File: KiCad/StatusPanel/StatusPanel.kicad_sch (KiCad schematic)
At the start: 37 parts, among them J1 CONN, J10 CONN_12V_CTL, J11 CONN_12V_GND, J12 CONN_TASK_CTL, J13 CONN_TASK_GND, J14 CONN_5V_CTL, J15 CONN_5V_GND, J16 CONN_COM_CTL, J17 CONN_COM_GND, J18 CONN_LOW_CTL, J19 CONN_LOW_GND, J2 CONN_RESET_CTL, J20 CONN_ERROR_CTL, J21 CONN_ERROR_GND, J22 CONN_7SEG, J3 CONN_RESET_GND, J4 CONN_USB_5V, J5 CONN_USB_CTL, J6 CONN_INPUT_CTL, J7 CONN_INPUT_GND, J8 CONN_RS485_CTL, J9 CONN_RS485_GND, U1 2281SB, U2 TM1637

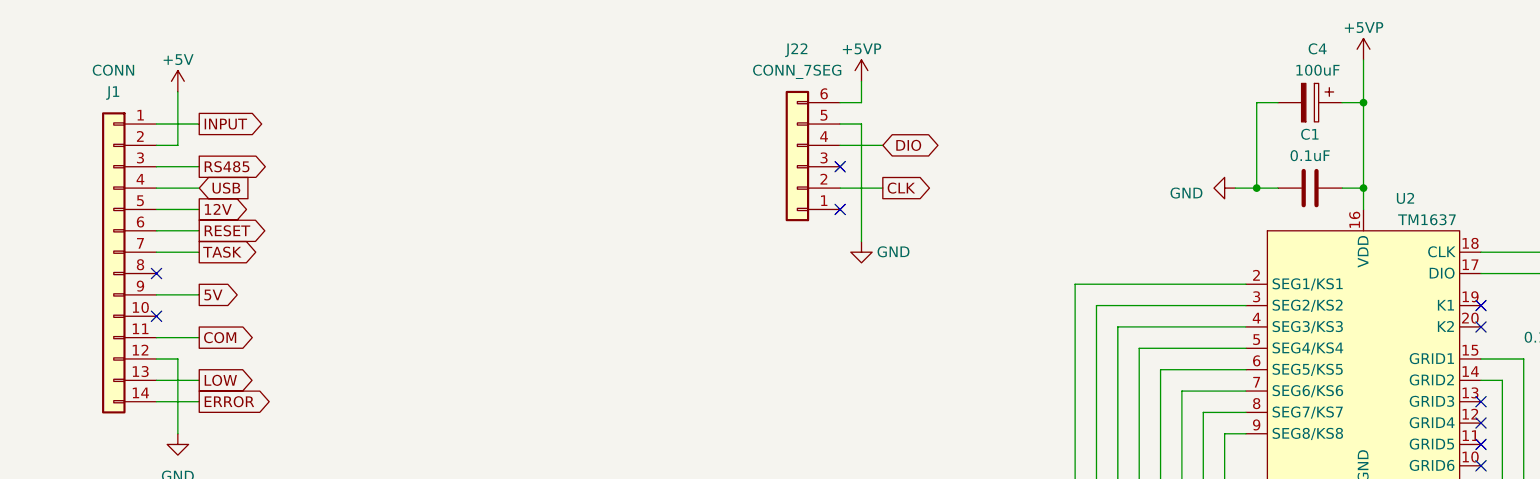
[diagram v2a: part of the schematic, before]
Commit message: 7セグ用コネクタを6Pから14Pの空いているピンに押し込んだ
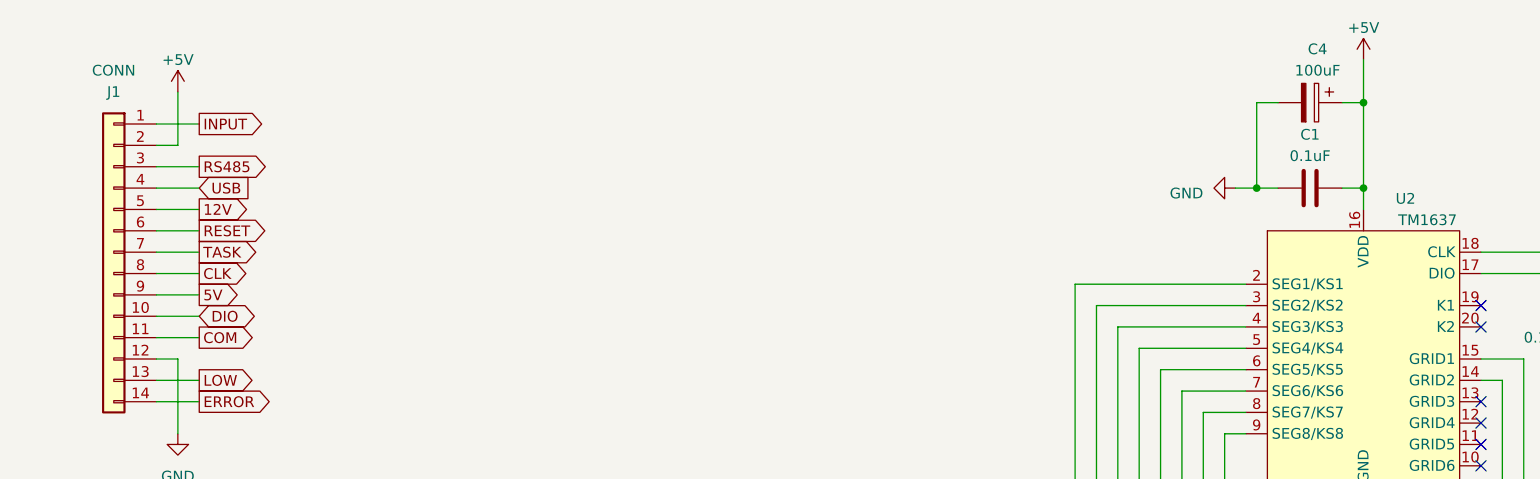
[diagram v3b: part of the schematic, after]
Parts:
- removed J22: CONN_7SEG, TSRP_Connector_Hirose:DF51A-6DP-2DSA, symbol Connector_Generic:Conn_01x06
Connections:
- net +5VP is gone; now on net +5V: C1.2, C4.1, U2.16 (VDD)
- net CLK: now also J1.8 (Pin_8)
- net DIO: now also J1.10 (Pin_10)
- no-connect marks 10 -> 6
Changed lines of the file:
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@@
   (junction (at 212.09 34.29) (diameter 0) (color 0 0 0 0)
   )
-  (no_connect (at 149.86 46.99))
   (no_connect (at 226.06 69.85))
-  (no_connect (at 68.58 59.69))
   (no_connect (at 226.06 58.42))
   (no_connect (at 226.06 74.93))
-  (no_connect (at 149.86 41.91))
   (no_connect (at 226.06 72.39))
   (no_connect (at 226.06 77.47))
-  (no_connect (at 68.58 54.61))
   (no_connect (at 226.06 60.96))
   (wire (pts (xy 53.34 149.86) (xy 55.88 149.86))
@@
     (stroke (width 0) (type default))
   )
+  (wire (pts (xy 68.58 54.61) (xy 73.66 54.61))
+    (stroke (width 0) (type default))
+  )
   (wire (pts (xy 209.55 44.45) (xy 212.09 44.45))
     (stroke (width 0) (type default))
   )
-  (wire (pts (xy 152.4 50.8) (xy 152.4 36.83))
-    (stroke (width 0) (type default))
-  )
   (wire (pts (xy 240.03 64.77) (xy 240.03 67.31))
     (stroke (width 0) (type default))
@@
     (stroke (width 0) (type default))
   )
-  (wire (pts (xy 149.86 36.83) (xy 152.4 36.83))
-    (stroke (width 0) (type default))
-  )
   (wire (pts (xy 53.34 109.22) (xy 55.88 109.22))
     (stroke (width 0) (type default))
@@
     (stroke (width 0) (type default))
   )
-  (wire (pts (xy 149.86 34.29) (xy 152.4 34.29))
-    (stroke (width 0) (type default))
-  )
   (wire (pts (xy 177.8 106.68) (xy 204.47 106.68))
     (stroke (width 0) (type default))
@@
     (stroke (width 0) (type default))
   )
-  (wire (pts (xy 149.86 39.37) (xy 154.94 39.37))
-    (stroke (width 0) (type default))
-  )
   (wire (pts (xy 198.12 73.66) (xy 195.58 73.66))
     (stroke (width 0) (type default))
@@
     (stroke (width 0) (type default))
   )
-  (wire (pts (xy 149.86 44.45) (xy 154.94 44.45))
-    (stroke (width 0) (type default))
-  )
   (wire (pts (xy 68.58 62.23) (xy 73.66 62.23))
     (stroke (width 0) (type default))
@@
     (stroke (width 0) (type default))
   )
-  (wire (pts (xy 152.4 31.75) (xy 152.4 34.29))
-    (stroke (width 0) (type default))
-  )
   (wire (pts (xy 226.06 67.31) (xy 228.6 67.31))
     (stroke (width 0) (type default))
@@
   )
   (wire (pts (xy 95.25 109.22) (xy 97.79 109.22))
+    (stroke (width 0) (type default))
+  )
+  (wire (pts (xy 68.58 59.69) (xy 73.66 59.69))
     (stroke (width 0) (type default))
   )
@@
     )
   )
+  (global_label "DIO" (shape bidirectional) (at 73.66 59.69 0) (fields_autoplaced)
+    (effects (font (size 1.27 1.27)) (justify left))
+    (property "Intersheetrefs" "${INTERSHEET_REFS}" (at 80.8824 59.69 0)
+      (effects (font (size 1.27 1.27)) (justify left) hide)
+    )
+  )
   (global_label "USB" (shape output) (at 97.79 109.22 0) (fields_autoplaced)
     (effects (font (size 1.27 1.27)) (justify left))
@@
     )
   )
+  (global_label "CLK" (shape output) (at 73.66 54.61 0) (fields_autoplaced)
+    (effects (font (size 1.27 1.27)) (justify left))
+    (property "Intersheetrefs" "${INTERSHEET_REFS}" (at 80.1339 54.61 0)
+      (effects (font (size 1.27 1.27)) (justify left) hide)
+    )
+  )
   (global_label "INPUT" (shape input) (at 43.18 123.19 180) (fields_autoplaced)
     (effects (font (size 1.27 1.27)) (justify right))
@@
     )
   )
-  (global_label "CLK" (shape output) (at 154.94 44.45 0) (fields_autoplaced)
-    (effects (font (size 1.27 1.27)) (justify left))
-    (property "Intersheetrefs" "${INTERSHEET_REFS}" (at 161.4139 44.45 0)
-      (effects (font (size 1.27 1.27)) (justify left) hide)
-    )
-  )
-  (global_label "DIO" (shape bidirectional) (at 154.94 39.37 0) (fields_autoplaced)
-    (effects (font (size 1.27 1.27)) (justify left))
-    (property "Intersheetrefs" "${INTERSHEET_REFS}" (at 162.1624 39.37 0)
-      (effects (font (size 1.27 1.27)) (justify left) hide)
-    )
-  )
   (global_label "TASK" (shape input) (at 43.18 149.86 180) (fields_autoplaced)
     (effects (font (size 1.27 1.27)) (justify right))
@@
         (path "/4e417ca2-390b-4eb8-b376-7083d40608de"
           (reference "C2") (unit 1)
-        )
-      )
-    )
-  )
-  (symbol (lib_id "power:+5VP") (at 212.09 29.21 0) (unit 1)
-    (in_bom yes) (on_board yes) (dnp no) (fields_autoplaced)
-    (property "Reference" "#PWR013" (at 212.09 33.02 0)
-      (effects (font (size 1.27 1.27)) hide)
-    )
-    (property "Value" "+5VP" (at 212.09 25.4 0)
-      (effects (font (size 1.27 1.27)))
-    )
-    (property "Footprint" "" (at 212.09 29.21 0)
-      (effects (font (size 1.27 1.27)) hide)
-    )
-    (property "Datasheet" "" (at 212.09 29.21 0)
-      (effects (font (size 1.27 1.27)) hide)
-    )
-    (pin "1")
-    (instances
-      (project "StatusPanel"
-        (path "/4e417ca2-390b-4eb8-b376-7083d40608de"
-          (reference "#PWR013") (unit 1)
         )
       )
@@
     )
   )
-  (symbol (lib_id "power:GND") (at 152.4 50.8 0) (mirror y) (unit 1)
-    (in_bom yes) (on_board yes) (dnp no)
-    (property "Reference" "#PWR014" (at 152.4 57.15 0)
-      (effects (font (size 1.27 1.27)) hide)
-    )
-    (property "Value" "GND" (at 156.21 52.07 0)
-      (effects (font (size 1.27 1.27)))
-    )
-    (property "Footprint" "" (at 152.4 50.8 0)
-      (effects (font (size 1.27 1.27)) hide)
-    )
-    (property "Datasheet" "" (at 152.4 50.8 0)
-      (effects (font (size 1.27 1.27)) hide)
-    )
-    (pin "1")
-    (instances
-      (project "StatusPanel"
-        (path "/4e417ca2-390b-4eb8-b376-7083d40608de"
-          (reference "#PWR014") (unit 1)
-        )
-      )
-      (project "LaunchController"
-        (path "/628d040b-43bf-4733-804f-091644a90124"
-          (reference "#PWR044") (unit 1)
-        )
-      )
-    )
-  )
   (symbol (lib_id "Connector_Generic:Conn_01x01") (at 60.96 158.75 0) (unit 1)
     (in_bom yes) (on_board yes) (dnp no)
@@
         (path "/4e417ca2-390b-4eb8-b376-7083d40608de"
           (reference "J10") (unit 1)
+        )
+      )
+    )
+  )
+  (symbol (lib_id "power:+5V") (at 212.09 29.21 0) (unit 1)
+    (in_bom yes) (on_board yes) (dnp no) (fields_autoplaced)
+    (property "Reference" "#PWR013" (at 212.09 33.02 0)
+      (effects (font (size 1.27 1.27)) hide)
+    )
+    (property "Value" "+5V" (at 212.09 25.4 0)
+      (effects (font (size 1.27 1.27)))
+    )
+    (property "Footprint" "" (at 212.09 29.21 0)
+      (effects (font (size 1.27 1.27)) hide)
+    )
+    (property "Datasheet" "" (at 212.09 29.21 0)
+      (effects (font (size 1.27 1.27)) hide)
+    )
+    (pin "1")
+    (instances
+      (project "StatusPanel"
+        (path "/4e417ca2-390b-4eb8-b376-7083d40608de"
+          (reference "#PWR013") (unit 1)
         )
       )
@@
     )
   )
-  (symbol (lib_id "Connector_Generic:Conn_01x06") (at 144.78 41.91 180) (unit 1)
-    (in_bom yes) (on_board yes) (dnp no)
-    (property "Reference" "J22" (at 144.78 27.94 0)
-      (effects (font (size 1.27 1.27)))
-    )
-    (property "Value" "CONN_7SEG" (at 144.78 30.48 0)
-      (effects (font (size 1.27 1.27)))
-    )
-    (property "Footprint" "TSRP_Connector_Hirose:DF51A-6DP-2DSA" (at 144.78 41.91 0)
-      (effects (font (size 1.27 1.27)) hide)
-    )
-    (property "Datasheet" "~" (at 144.78 41.91 0)
-      (effects (font (size 1.27 1.27)) hide)
-    )
-    (pin "1")
-    (pin "2")
-    (pin "3")
-    (pin "4")
-    (pin "5")
-    (pin "6")
-    (instances
-      (project "StatusPanel"
-        (path "/4e417ca2-390b-4eb8-b376-7083d40608de"
-          (reference "J22") (unit 1)
-        )
-      )
-      (project "LaunchController"
-        (path "/628d040b-43bf-4733-804f-091644a90124"
-          (reference "J13") (unit 1)
-        )
-      )
-    )
-  )
   (symbol (lib_id "Connector_Generic:Conn_01x01") (at 80.01 140.97 180) (unit 1)
     (in_bom yes) (on_board yes) (dnp no) (fields_autoplaced)
@@
         )
       )
-    )
-  )
-  (symbol (lib_id "power:+5VP") (at 152.4 31.75 0) (unit 1)
-    (in_bom yes) (on_board yes) (dnp no) (fields_autoplaced)
-    (property "Reference" "#PWR020" (at 152.4 35.56 0)
-      (effects (font (size 1.27 1.27)) hide)
-    )
-    (property "Value" "+5VP" (at 152.4 27.94 0)
-      (effects (font (size 1.27 1.27)))
-    )
-    (property "Footprint" "" (at 152.4 31.75 0)
-      (effects (font (size 1.27 1.27)) hide)
-    )
-    (property "Datasheet" "" (at 152.4 31.75 0)
-      (effects (font (size 1.27 1.27)) hide)
-    )
-    (pin "1")
-    (instances
-      (project "StatusPanel"
-        (path "/4e417ca2-390b-4eb8-b376-7083d40608de"
-          (reference "#PWR020") (unit 1)
-        )
-      )

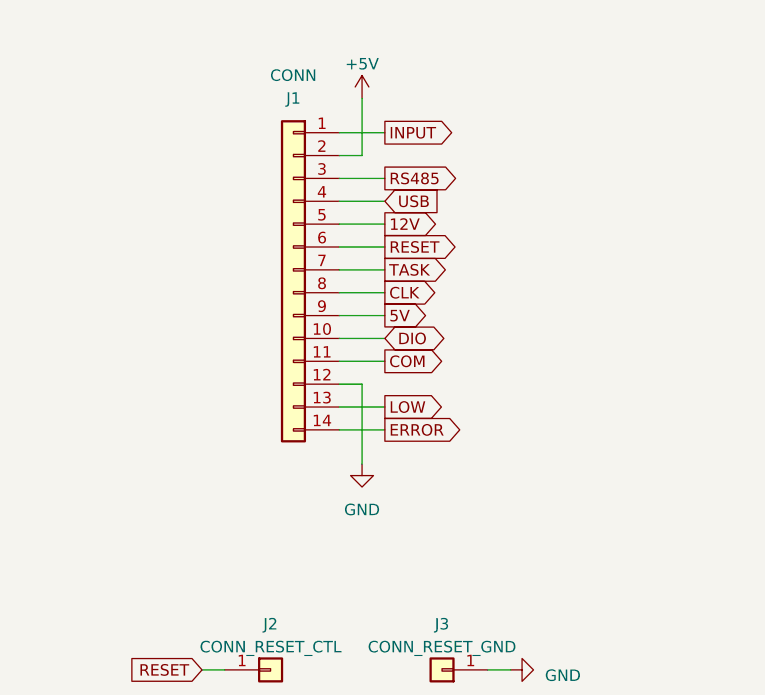
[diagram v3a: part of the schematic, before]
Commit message: ステータスパネルのコネクタをDF11に変更
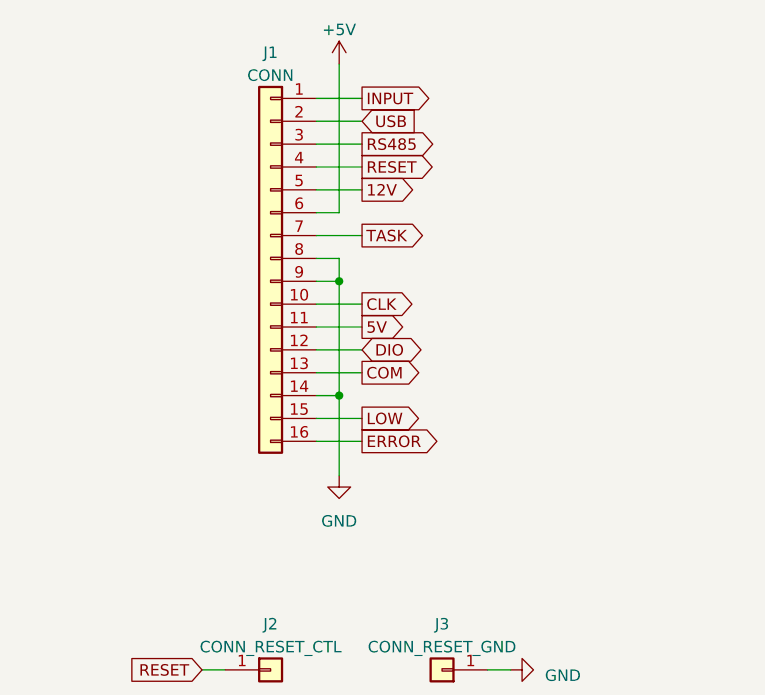
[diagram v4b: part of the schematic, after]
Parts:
- removed J1: CONN, TSRP_Connector_Hirose:DF51A-14DP-2DS, symbol Connector_Generic:Conn_01x14
- added J1: CONN, TSRP_Connector_Hirose:DF11CZ-16DP-2V, symbol Connector_Generic:Conn_01x16
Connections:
- net +5V: now also J1.6 (Pin_6)
- net 12V: now also J1.5 (Pin_5)
- net 5V: now also J1.11 (Pin_11)
- net CLK: now also J1.10 (Pin_10)
- net COM: now also J1.13 (Pin_13)
- net DIO: now also J1.12 (Pin_12)
- net ERROR: now also J1.16 (Pin_16)
- net GND: now also J1.14 (Pin_14), J1.8 (Pin_8), J1.9 (Pin_9)
- net INPUT: now also J1.1 (Pin_1)
- net LOW: now also J1.15 (Pin_15)
- net RESET: now also J1.4 (Pin_4)
- net RS485: now also J1.3 (Pin_3)
- net TASK: now also J1.7 (Pin_7)
- net USB: now also J1.2 (Pin_2)
